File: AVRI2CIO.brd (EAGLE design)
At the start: 99.1 x 78.7 mm, 39 parts, among them IC1 MEGA8-P

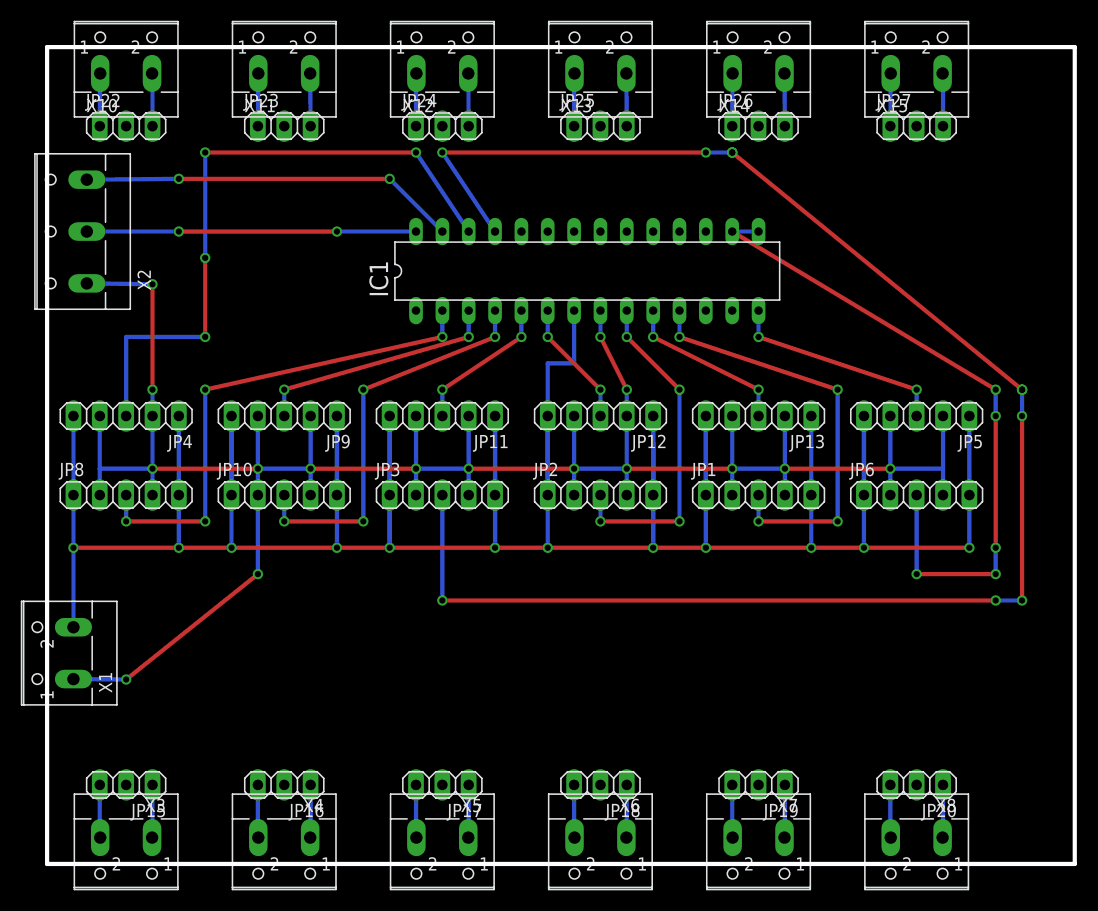
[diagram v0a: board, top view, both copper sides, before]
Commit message: Schema  rename some items Board   move some items -> now 12 IO + I2C + Power connectors
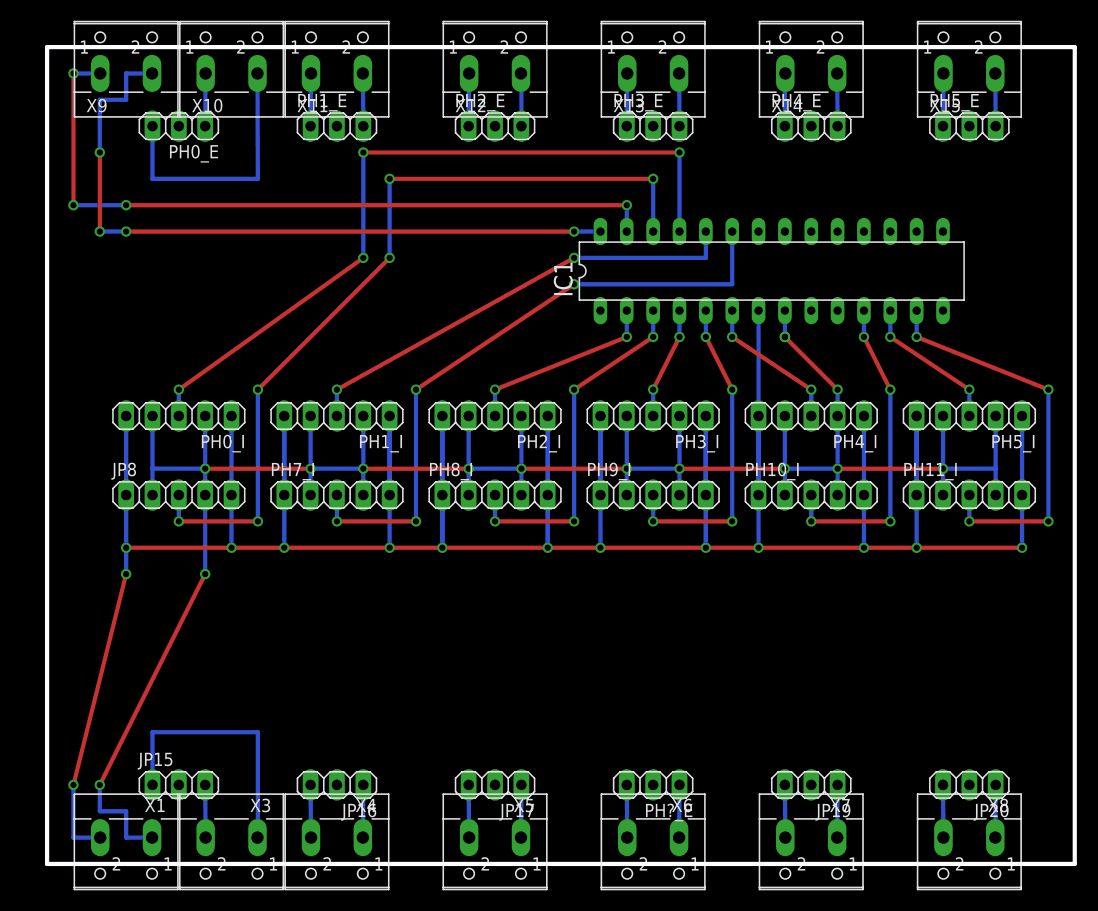
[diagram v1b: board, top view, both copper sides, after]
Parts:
- removed JP1, JP10, JP11, JP12, JP13, JP2, JP3, JP4, JP5, JP6, JP9: (no value), pinhead:1X05
- removed JP18, JP22, JP23, JP24, JP25, JP26, JP27: (no value), pinhead:1X03
- removed X2: (no value), con-wago-500:W237-103
- added PH0_E, PH1_E, PH2_E, PH3_E, PH4_E, PH5_E, PH?_E: (no value), pinhead:1X03
- added PH0_I, PH10_I, PH11_I, PH1_I, PH2_I, PH3_I, PH4_I, PH5_I, PH7_I, PH8_I, PH9_I: (no value), pinhead:1X05
- added X9: (no value), con-wago-500:W237-102
- moved X1 20.1 mm to (7.62, 1.27), turned to 180 degrees
- moved IC1 17.8 mm to (69.8, 57.1)
- moved X10 10.2 mm to (17.8, 77.5)
- moved X3 10.2 mm to (17.8, 1.27)
- moved JP20 5.08 mm to (88.9, 7.62)
- moved X15 5.08 mm to (88.9, 77.5)
- moved X8 5.08 mm to (88.9, 1.27)
- moved JP16 5.08 mm to (27.9, 7.62)
- moved X11 5.08 mm to (27.9, 77.5)
- moved X4 5.08 mm to (27.9, 1.27)
- moved JP15 5.08 mm to (12.7, 7.62), turned to 0 degrees
- moved JP8 5.08 mm to (12.7, 35.6)
- moved JP17 5.08 mm to (43.2, 7.62)
- moved JP19 5.08 mm to (73.7, 7.62)
- moved X12 5.08 mm to (43.2, 77.5)
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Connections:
- removed net IO0: IC1.11, JP1.3
- removed net IO10: IC1.4, JP10.3
- removed net IO11: IC1.5, JP11.3
- removed net IO12: IC1.6, JP12.3
- removed net IO14: IC1.12
- removed net IO15: IC1.13
- removed net IO2: IC1.25, JP3.3
- removed net IO3: IC1.26, JP4.3
- removed net IO4: IC1.14, JP5.3
- removed net IO5: IC1.15, JP6.3
- removed net IO6: IC1.16
- removed net IO7: IC1.17
- removed net IO8: IC1.2, JP8.3
- removed net IO9: IC1.3, JP9.3
- removed net N$18: JP22.3, X10.2
- removed net N$2: IC1.1
- removed net N$21: IC1.18
- removed net N$22: IC1.19
- removed net N$32: IC1.23
- new net PC0: IC1.23, PH7_I.3
- new net PC1: IC1.24, PH1_I.3
- new net PC2: IC1.25, PH0_I.3
- new net PC3: IC1.26, JP8.3
- new net PD0: IC1.2, PH2_I.3
- new net PD1: IC1.3, PH8_I.3
- new net PD2: IC1.4, PH3_I.3
- new net PD3: IC1.5, PH9_I.3
- new net PD4: IC1.6, PH4_I.3
- new net PD5: IC1.11, PH10_I.3
- new net PD6: IC1.12, PH5_I.3
- new net PD7: IC1.13, PH11_I.3
- net +5V: now also PH0_I.1, PH0_I.5, PH10_I.1, PH10_I.5, PH11_I.1, PH11_I.5, PH1_I.1, PH1_I.5, PH2_I.1, PH2_I.5, PH3_I.1, PH3_I.5, PH4_I.1, PH4_I.5, PH5_I.1, PH5_I.5, PH7_I.1, PH7_I.5, PH8_I.1, PH8_I.5, PH9_I.1, PH9_I.5; no longer JP1.1, JP1.5, JP10.1, JP10.5, JP11.1, JP11.5, JP12.1, JP12.5, JP13.1, JP13.5, JP2.1, JP2.5, JP3.1, JP3.5, JP4.1, JP4.5, JP5.1, JP5.5, JP6.1, JP6.5, JP9.1, JP9.5
- net GND: now also PH0_I.2, PH0_I.4, PH10_I.2, PH10_I.4, PH11_I.2, PH11_I.4, PH1_I.2, PH1_I.4, PH2_I.2, PH2_I.4, PH3_I.2, PH3_I.4, PH4_I.2, PH4_I.4, PH5_I.2, PH5_I.4, PH7_I.2, PH7_I.4, PH8_I.2, PH8_I.4, PH9_I.2, PH9_I.4; no longer JP1.2, JP1.4, JP10.2, JP10.4, JP11.2, JP11.4, JP12.2, JP12.4, JP13.2, JP13.4, JP2.2, JP2.4, JP3.2, JP3.4, JP4.2, JP4.4, JP5.2, JP5.4, JP6.2, JP6.4, JP9.2, JP9.4, X2.1
- net IO1: no longer JP2.3
- net IO13: no longer JP13.3
- net N$1: now also PH0_E.3, X10.2; no longer IC1.24
- net N$10: now also PH?_E.1; no longer JP18.1
- net N$17: now also PH0_E.1; no longer JP22.1
- net N$19: now also PH1_E.1; no longer JP23.1
- net N$20: now also PH1_E.3; no longer JP23.3
- net N$23: now also PH2_E.1; no longer JP24.1
- net N$24: now also PH2_E.3; no longer JP24.3
- net N$25: now also PH3_E.1; no longer JP25.1
- net N$26: now also PH3_E.3; no longer JP25.3
- net N$27: now also PH4_E.1; no longer JP26.1
- net N$28: now also PH4_E.3; no longer JP26.3
- net N$29: now also PH5_E.1; no longer JP27.1
- net N$30: now also PH5_E.3; no longer JP27.3
- net N$9: now also PH?_E.3; no longer JP18.3
- net SCL: now also X9.2; no longer X2.2
- net SDA: now also X9.1; no longer X2.3
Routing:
- net IO2: track 159.6 -> 0.00 mm, vias 10 -> 0
- net PC3: track 0.00 -> 78.9 mm, vias 0 -> 6
- net PC2: track 0.00 -> 72.6 mm, vias 0 -> 4
- net IO5: track 65.2 -> 0.00 mm, vias 6 -> 0
- net IO3: track 62.5 -> 0.00 mm, vias 4 -> 0
- net PC0: track 0.00 -> 61.5 mm, vias 0 -> 4
- net IO8: track 48.8 -> 0.00 mm, vias 4 -> 0
- net PC1: track 0.00 -> 43.9 mm, vias 0 -> 2
- net IO0: track 41.5 -> 0.00 mm, vias 4 -> 0
- net IO10: track 39.1 -> 0.00 mm, vias 4 -> 0
- net PD7: track 0.00 -> 39.1 mm, vias 0 -> 4
- net SCL: track 31.7 -> 68.5 mm, vias 2 -> 4
- net SDA: track 36.4 -> 71.2 mm, vias 2 -> 4
- net PD1: track 0.00 -> 34.6 mm, vias 0 -> 4
- net IO1: track 32.6 -> 0.00 mm, vias 4 -> 0
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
